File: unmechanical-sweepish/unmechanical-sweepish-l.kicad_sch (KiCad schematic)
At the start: 82 parts, among them J6 M, Q2 AO3400A, U10 74HC4051, U4 OPA340NA

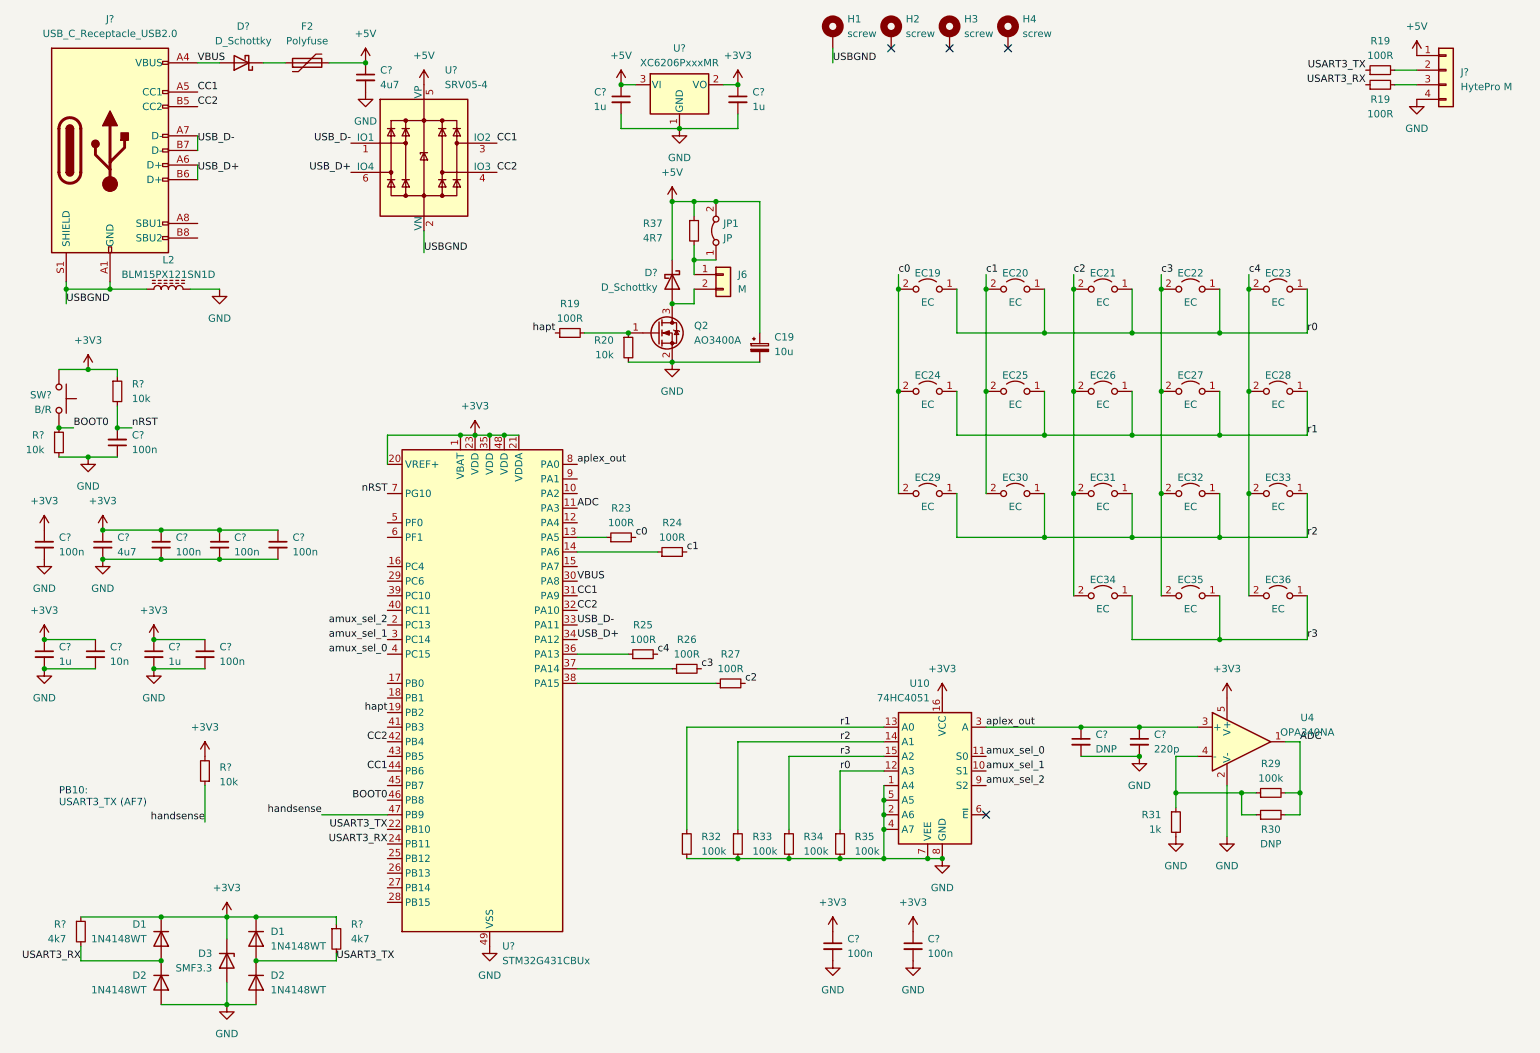
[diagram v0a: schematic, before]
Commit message: update to kicad 8 model paths
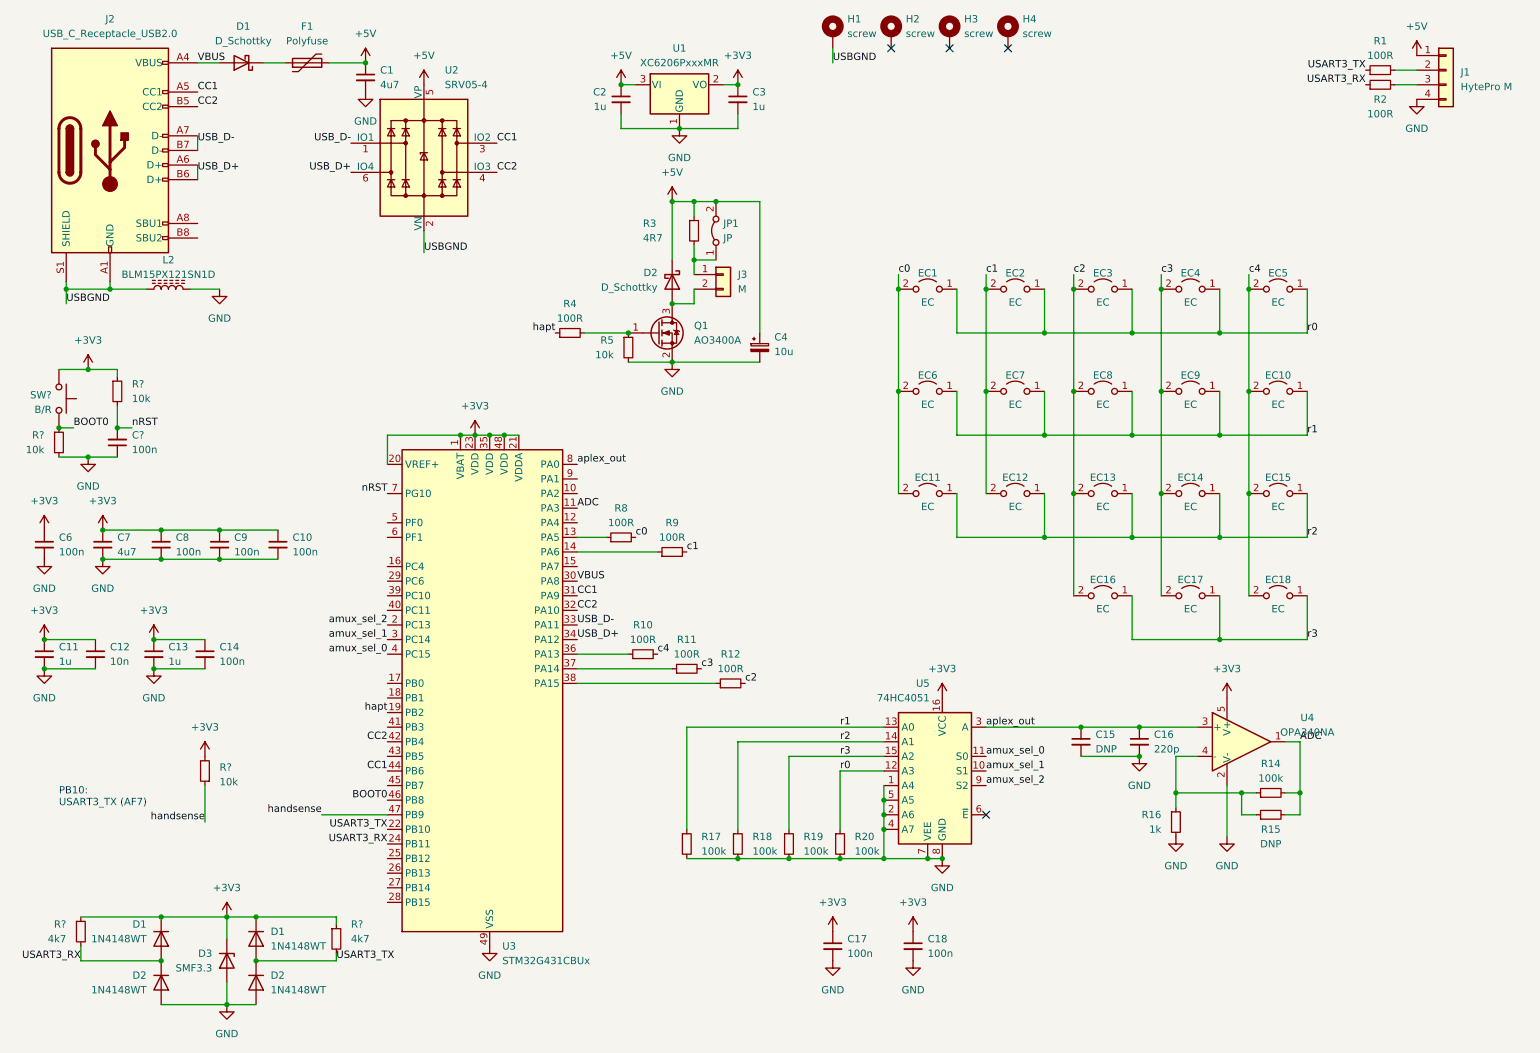
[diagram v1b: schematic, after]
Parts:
- J1: renamed from J?; footprint PCM_marbastlib-xp-various:CON_HytePro_M411P_Plug_1x04-P2.20mm_Horizontal_FlushMount -> PCM_marbastlib-various:CON_HytePro_M411P_Plug_1x04-P2.20mm_Horizontal_FlushMount
- L2: value BLM15PX121SN1D -> BLM15PX121SN1D
- gave numbers to parts that had none: 22
- renumbered C19 to C4, EC19 to EC1, EC28 to EC10, EC29 to EC11, EC30 to EC12, EC31 to EC13, EC32 to EC14, EC33 to EC15, EC34 to EC16, EC35 to EC17, EC36 to EC18, EC20 to EC2, EC21 to EC3, EC22 to EC4, EC23 to EC5, EC24 to EC6, EC25 to EC7, EC26 to EC8, EC27 to EC9, F2 to F1, J6 to J3, Q2 to Q1, R19 to R1, R25 to R10, R26 to R11, R27 to R12, R29 to R14, R30 to R15, R31 to R16, R32 to R17, R33 to R18, R34 to R19, R19 to R2, R35 to R20, R37 to R3, R19 to R4, R20 to R5, R23 to R8, R24 to R9, U10 to U5
